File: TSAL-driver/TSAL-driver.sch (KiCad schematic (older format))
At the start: 16 parts

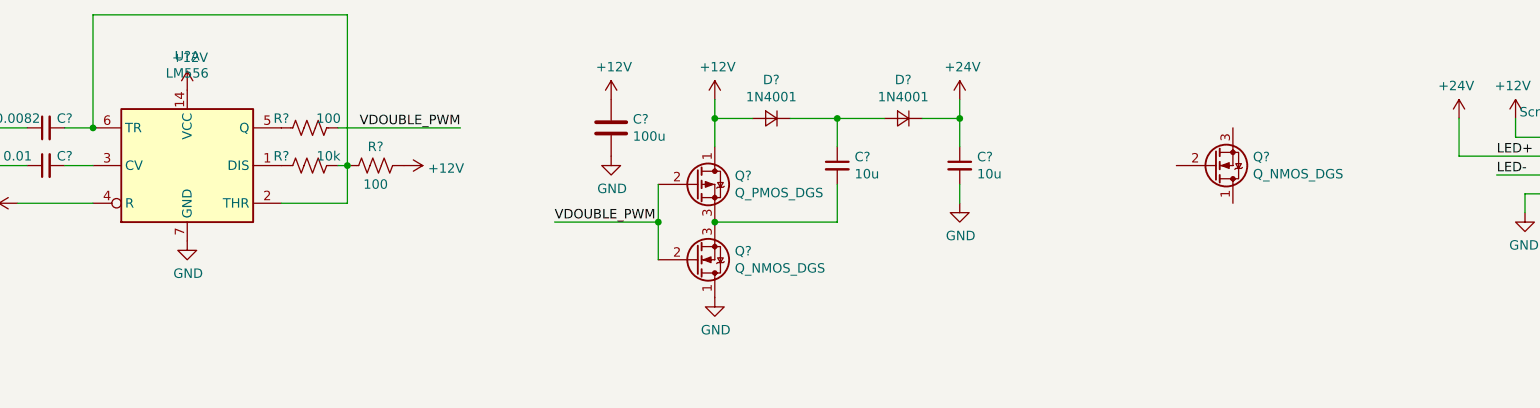
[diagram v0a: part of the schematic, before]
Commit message: Drew fet inverter
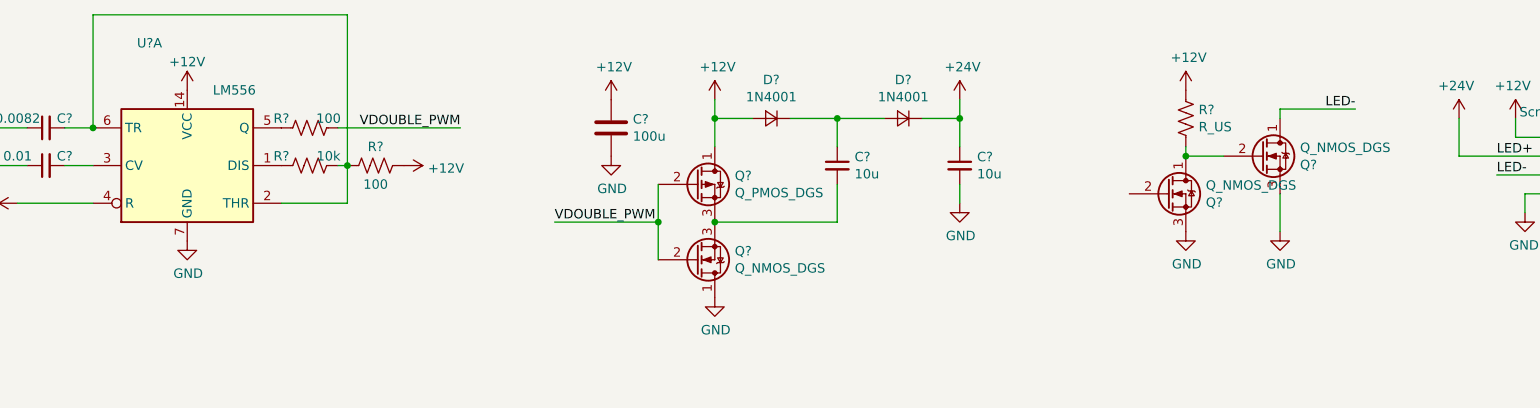
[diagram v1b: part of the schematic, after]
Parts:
- added Q?: Q_NMOS_DGS, symbol Device:Q_NMOS_DGS
- added R?: R_US, symbol Device:R_US
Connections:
- net +12V: now also R?.1
- net GND: now also Q?.3 (S), Q?.3 (S)
- net LED-: now also Q?.1 (D)
- net at Q?.1 (D): now also Q?.2 (G), R?.2
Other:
- moved on the sheet: Q?
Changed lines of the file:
@@
 EESchema Schematic File Version 4
+LIBS:TSAL-driver-cache
 EELAYER 29 0
 EELAYER END
@@
 U 1 1 5CD0CC47
 P 3300 2500
-F 0 "U?" H 3300 3081 50  0000 C CNN
-F 1 "LM556" H 3300 2990 50  0000 C CNN
+F 0 "U?" H 3100 3150 50  0000 C CNN
+F 1 "LM556" H 3550 2900 50  0000 C CNN
 F 2 "" H 3300 2500 50  0001 C CNN
 F 3 "http://www.ti.com/lit/ds/symlink/lm556.pdf" H 3300 2500 50  0001 C CNN
@@
 P 3300 2100
 F 0 "#PWR?" H 3300 1950 50  0001 C CNN
-F 1 "+12V" H 3315 2273 50  0000 C CNN
+F 1 "+12V" H 3300 2250 50  0000 C CNN
 F 2 "" H 3300 2100 50  0001 C CNN
 F 3 "" H 3300 2100 50  0001 C CNN
@@
 $EndComp
 $Comp
-L Device:Q_NMOS_DGS Q?
-U 1 1 5CD39BB5
-P 8750 2500
-F 0 "Q?" H 8956 2454 50  0000 L CNN
-F 1 "Q_NMOS_DGS" H 8956 2545 50  0000 L CNN
-F 2 "" H 8950 2600 50  0001 C CNN
-F 3 "~" H 8750 2500 50  0001 C CNN
-	1    8750 2500
-	1    0    0    1
-$EndComp
-$Comp
 L Connector:Screw_Terminal_01x04 J?
 U 1 1 5CD3D4B5
@@
 Wire Wire Line
 	10650 2450 10050 2450
+$Comp
+L Device:Q_NMOS_DGS Q?
+U 1 1 5D129610
+P 9000 2450
+F 0 "Q?" H 9206 2404 50  0000 L CNN
+F 1 "Q_NMOS_DGS" H 9206 2495 50  0000 L CNN
+F 2 "" H 9200 2550 50  0001 C CNN
+F 3 "~" H 9000 2450 50  0001 C CNN
+	1    9000 2450
+	1    0    0    -1
+$EndComp
+$Comp
+L power:GND #PWR?
+U 1 1 5D12C7B7
+P 9100 2850
+F 0 "#PWR?" H 9100 2600 50  0001 C CNN
+F 1 "GND" H 9105 2677 50  0000 C CNN
+F 2 "" H 9100 2850 50  0001 C CNN
+F 3 "" H 9100 2850 50  0001 C CNN
+	1    9100 2850
+	1    0    0    -1
+$EndComp
+Wire Wire Line
+	9100 2250 9100 2200
+Wire Wire Line
+	9100 2200 9500 2200
+Text Label 9500 2200 2    50   ~ 0
+LED-
+Wire Wire Line
+	8600 2450 8800 2450
+$Comp
+L power:GND #PWR?
+U 1 1 5D131787
+P 8600 2850
+F 0 "#PWR?" H 8600 2600 50  0001 C CNN
+F 1 "GND" H 8605 2677 50  0000 C CNN
+F 2 "" H 8600 2850 50  0001 C CNN
+F 3 "" H 8600 2850 50  0001 C CNN
+	1    8600 2850
+	1    0    0    -1
+$EndComp
+Wire Wire Line
+	9100 2650 9100 2850
+$Comp
+L Device:R_US R?
+U 1 1 5D132ECB
+P 8600 2250
+F 0 "R?" H 8668 2296 50  0000 L CNN
+F 1 "R_US" H 8668 2205 50  0000 L CNN
+F 2 "" V 8640 2240 50  0001 C CNN
+F 3 "~" H 8600 2250 50  0001 C CNN
+	1    8600 2250
+	1    0    0    -1
+$EndComp
+Wire Wire Line
+	8600 2400 8600 2450
+Connection ~ 8600 2450
+$Comp
+L Device:Q_NMOS_DGS Q?
+U 1 1 5CD39BB5
+P 8500 2650
+F 0 "Q?" H 8706 2604 50  0000 L CNN
+F 1 "Q_NMOS_DGS" H 8706 2695 50  0000 L CNN
+F 2 "" H 8700 2750 50  0001 C CNN
+F 3 "~" H 8500 2650 50  0001 C CNN
+	1    8500 2650
+	1    0    0    -1
+$EndComp
+$Comp
+L power:+12V #PWR?
+U 1 1 5D135F72
+P 8600 2100
+F 0 "#PWR?" H 8600 1950 50  0001 C CNN
+F 1 "+12V" H 8615 2273 50  0000 C CNN
+F 2 "" H 8600 2100 50  0001 C CNN
+F 3 "" H 8600 2100 50  0001 C CNN
+	1    8600 2100
+	1    0    0    -1
+$EndComp
 $EndSCHEMATC

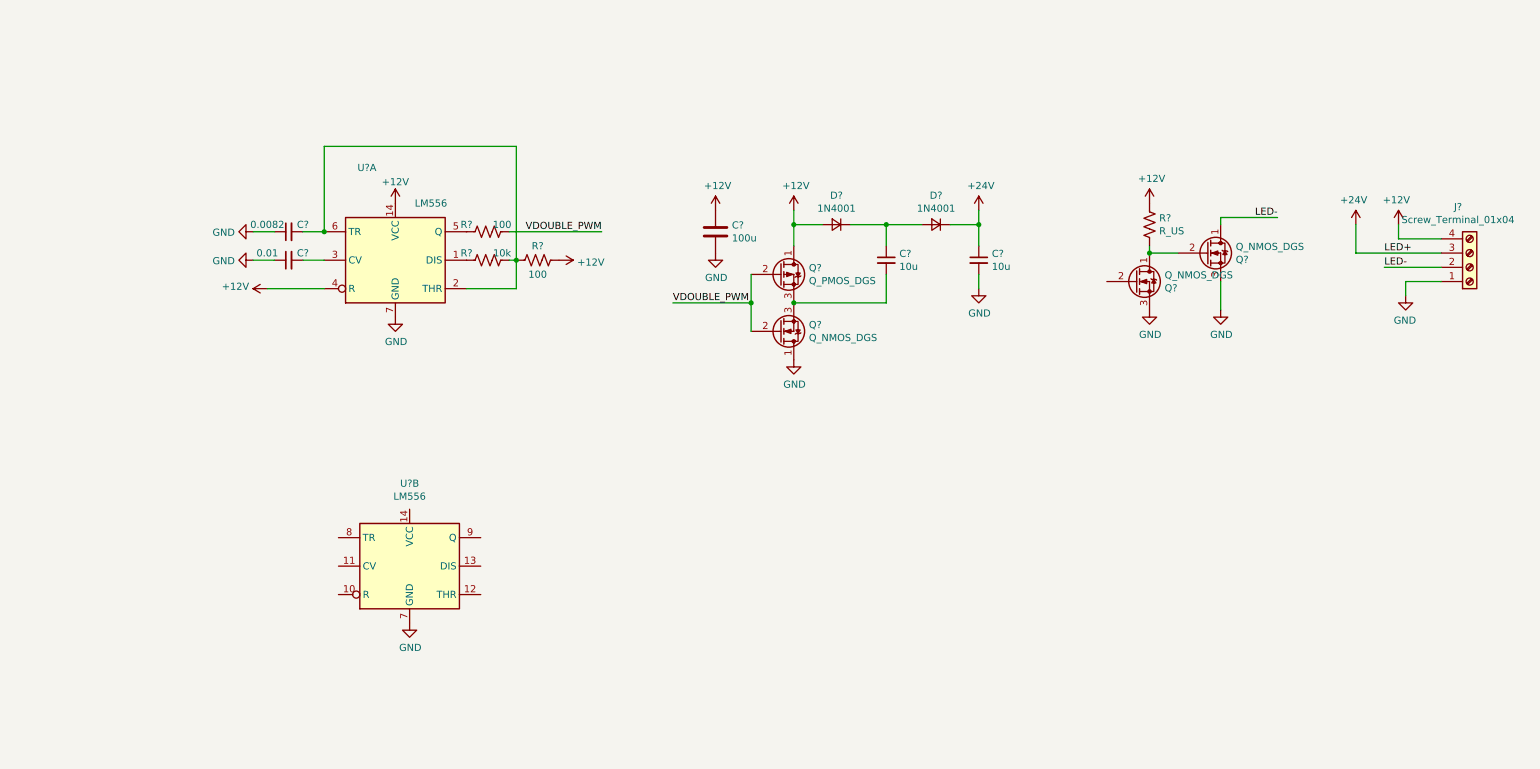
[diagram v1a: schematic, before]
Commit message: More work on TSAL-driver.
TODO: Get actual values in for both 555 circuits.
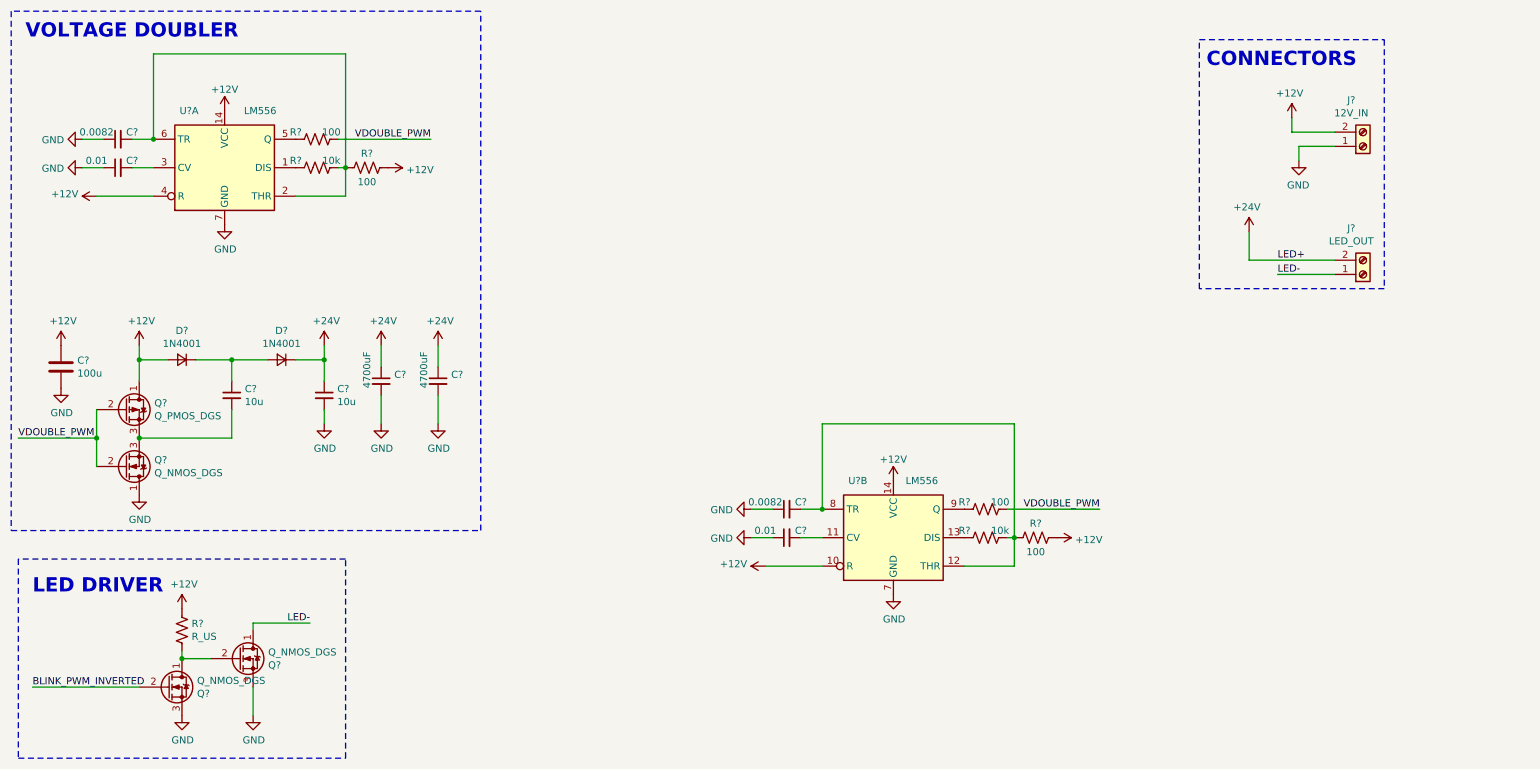
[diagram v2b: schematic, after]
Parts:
- removed J?: Screw_Terminal_01x04, symbol Connector:Screw_Terminal_01x04
- added C? (x2): 4700uF, symbol Device:C_Small
- added C?: 0.0082, symbol Device:C_Small
- added C?: 0.01, symbol Device:C_Small
- added J?: LED_OUT, LED_OUT, symbol Connector:Screw_Terminal_01x02
- added J?: 12V_IN, LED_OUT, symbol Connector:Screw_Terminal_01x02
- added R? (x2): 100, symbol Device:R_US
- added R?: 10k, symbol Device:R_US
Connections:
- net +12V: now also U?.10 (R), U?.14 (VCC), J?.2 (Pin_2), R?.1
- net +24V: now also C?.1, C?.1, J?.2 (Pin_2)
- net GND: now also C?.1, C?.1, C?.2, C?.2, J?.1 (Pin_1)
- net LED-: now also J?.1 (Pin_1)
- net VDOUBLE_PWM: now also R?.1
- net at U?.11 (CV): now also C?.2
- net at U?.12 (THR): now also U?.8 (TR), C?.2, R?.2, R?.2
- net at U?.13 (DIS): now also R?.1
- net at U?.9 (Q): now also R?.2
- net BLINK_PWM_INVERTED: now reaches Q?.2 (G)
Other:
- note added: "CONNECTORS"
- note added: "LED DRIVER"
- note added: "VOLTAGE DOUBLER"
- moved on the sheet: C?, D?, Q?, R?, U?A, U?B

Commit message: TODO: update values for 555 blinker
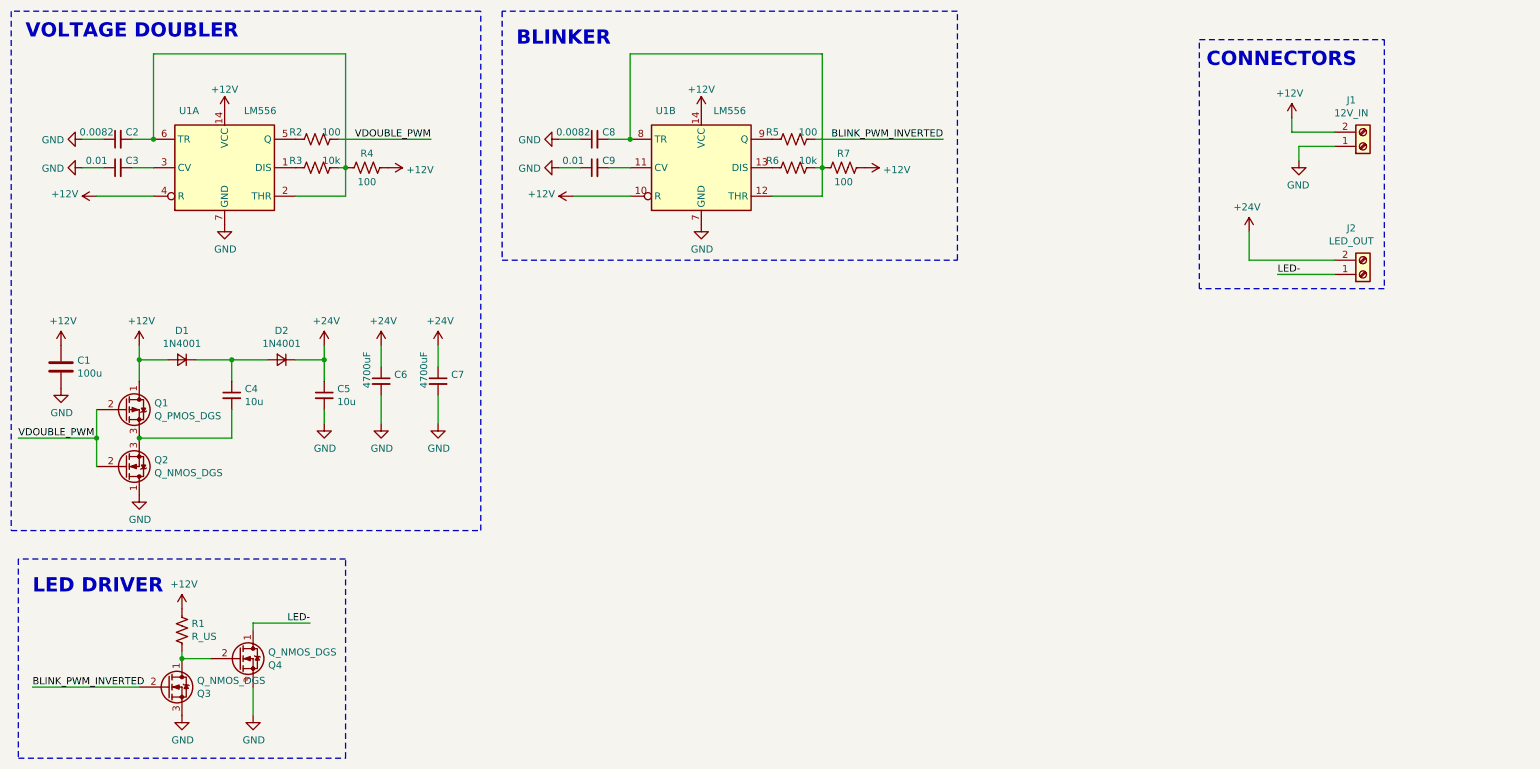
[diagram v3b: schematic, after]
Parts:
- gave numbers to parts that had none: 25
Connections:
- net BLINK_PWM_INVERTED: now also R5.1
- net VDOUBLE_PWM: no longer R5.1
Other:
- note added: "BLINKER"
- moved on the sheet: C8, C9, R5, R6, R7, U1B

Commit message: Beginning of can-game-controller
An interface to drive a simulator with the real car.
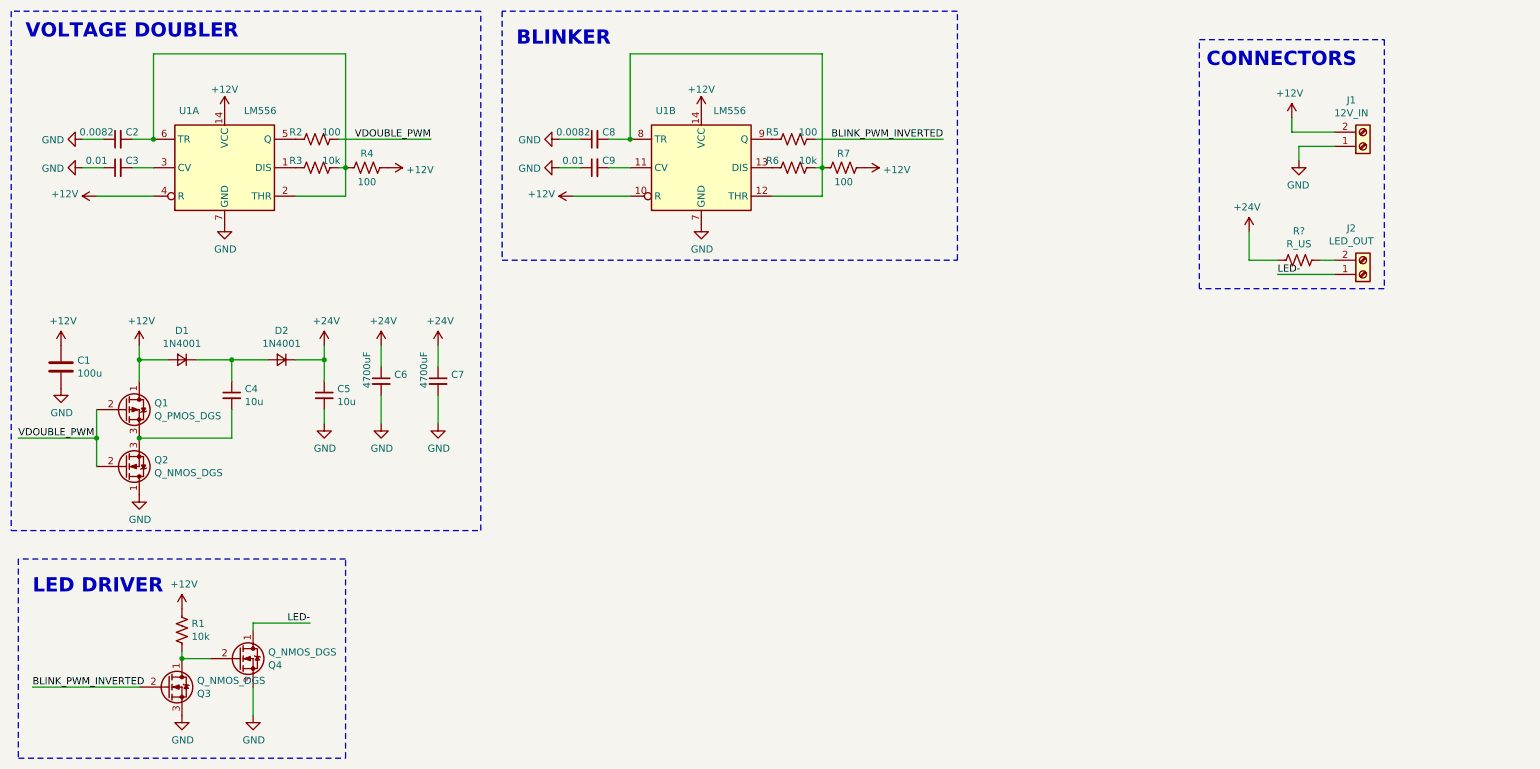
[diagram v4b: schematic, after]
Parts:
- added R?: R_US, symbol Device:R_US
- R1: value R_US -> 10k
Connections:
- net +24V: now also R?.2; no longer J2.2 (Pin_2)
- new net: J2.2 (Pin_2), R?.1
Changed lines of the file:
@@
 $EndComp
-Wire Wire Line
-	9900 1600 9600 1600
 Wire Wire Line
 	9600 1600 9600 1500
@@
 Wire Wire Line
 	9300 2300 9300 2500
-Wire Wire Line
-	9900 2500 9300 2500
 $Comp
 L Device:Q_NMOS_DGS Q4
@@
 P 1800 5100
 F 0 "R1" H 1868 5146 50  0000 L CNN
-F 1 "R_US" H 1868 5055 50  0000 L CNN
+F 1 "10k" H 1868 5055 50  0000 L CNN
 F 2 "" V 1840 5090 50  0001 C CNN
 F 3 "~" H 1800 5100 50  0001 C CNN
@@
 Text Notes 4150 1000 0    100  ~ 20
 BLINKER
+Wire Wire Line
+	9900 1600 9600 1600
+$Comp
+L Device:R_US R?
+U 1 1 5D55FF69
+P 9650 2500
+F 0 "R?" V 9445 2500 50  0000 C CNN
+F 1 "R_US" V 9536 2500 50  0000 C CNN
+F 2 "" V 9690 2490 50  0001 C CNN
+F 3 "~" H 9650 2500 50  0001 C CNN
+	1    9650 2500
+	0    1    1    0
+$EndComp
+Wire Wire Line
+	9300 2500 9500 2500
+Wire Wire Line
+	9800 2500 9900 2500
 $EndSCHEMATC
